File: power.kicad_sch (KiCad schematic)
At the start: 40 parts, among them T1 net-tie, U2 TPS546D24ARVFR

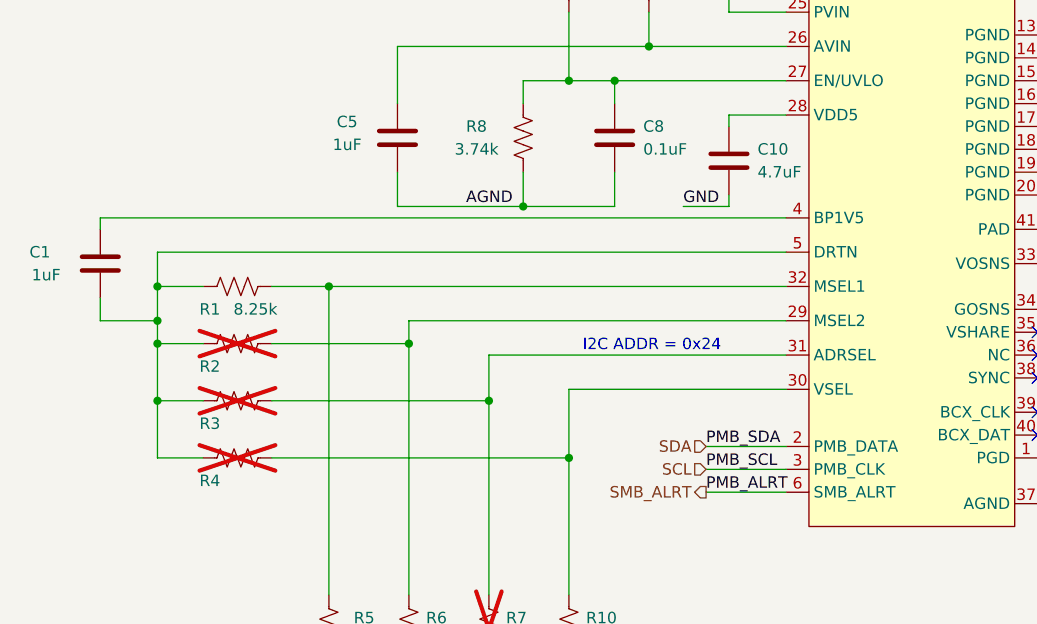
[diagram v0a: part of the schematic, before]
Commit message: swapped some parts numbers and packages for #169, DFM Improvements
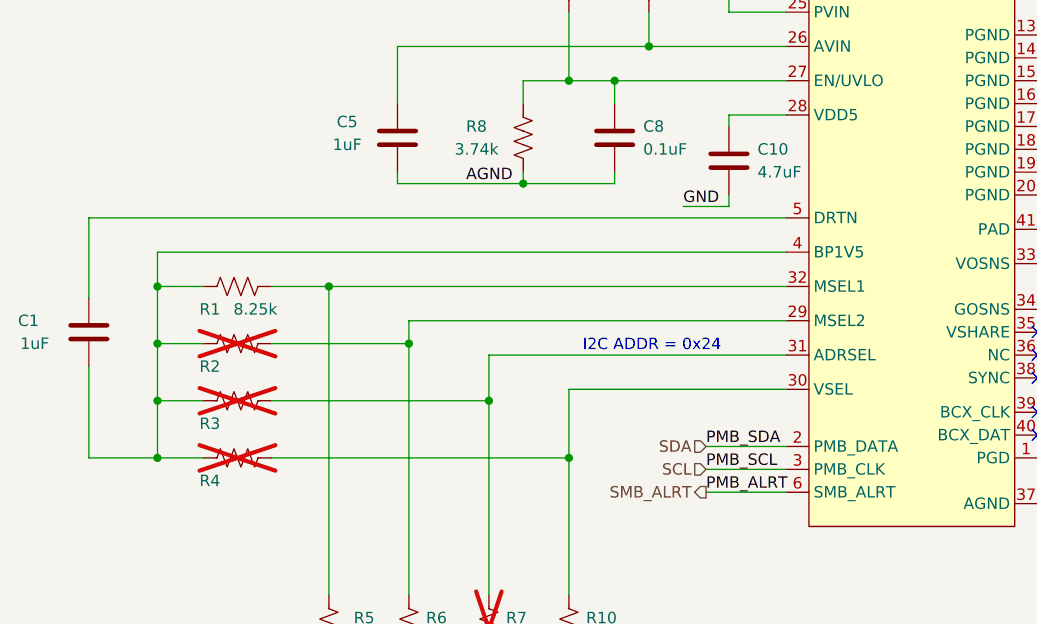
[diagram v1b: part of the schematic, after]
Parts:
- C1: footprint Capacitor_SMD:C_0603_1608Metric -> Capacitor_SMD:C_0402_1005Metric; DK 490-1550-1-ND -> 587-5514-1-ND; PARTNO GRM188R60J105KA01D -> EMK105BJ105MV-F
- C17, C18, C19, C20: footprint Capacitor_SMD:C_1210_3225Metric -> Capacitor_SMD:C_1206_3216Metric; DK 490-6533-1-ND -> 445-6008-1-ND; PARTNO GRM32EC80J107ME20L -> C3216X5R0J107M160AB
- C2: footprint Capacitor_SMD:C_1206_3216Metric -> Capacitor_SMD:C_0805_2012Metric; DK 1276-3038-1-ND -> 1276-1096-1-ND; PARTNO CL31A106KAHNFNE -> CL21A106KOQNNNE
- C5, C7: footprint Capacitor_SMD:C_0805_2012Metric -> Capacitor_SMD:C_0402_1005Metric; DK 587-1291-1-ND -> 587-5514-1-ND; PARTNO TMK212BJ105KG-T -> EMK105BJ105MV-F
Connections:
- net at C1.1: now also U2.5 (DRTN); no longer U2.4 (BP1V5)
- net at C1.2, R1.1, R2.1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: now also U2.4 (BP1V5); no longer U2.5 (DRTN)
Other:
- moved on the sheet: C1

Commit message: silkscreen cleanup
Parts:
- C17, C18, C19, C20: DK 445-6008-1-ND -> 490-GRM31CR61A107MEA8LCT-ND; PARTNO C3216X5R0J107M160AB -> GRM31CR61A107MEA8L
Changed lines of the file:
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@@
 			)
 		)
-		(property "DK" "445-6008-1-ND"
+		(property "DK" "490-GRM31CR61A107MEA8LCT-ND"
 			(at 224.79 68.58 0)
 			(effects
@@
 			)
 		)
-		(property "PARTNO" "C3216X5R0J107M160AB"
+		(property "PARTNO" "GRM31CR61A107MEA8L"
 			(at 224.79 68.58 0)
 			(effects
@@
 			)
 		)
-		(property "DK" "445-6008-1-ND"
+		(property "DK" "490-GRM31CR61A107MEA8LCT-ND"
 			(at 214.63 60.96 0)
 			(effects
@@
 			)
 		)
-		(property "PARTNO" "C3216X5R0J107M160AB"
+		(property "PARTNO" "GRM31CR61A107MEA8L"
 			(at 214.63 60.96 0)
 			(effects
@@
 			)
 		)
-		(property "DK" "445-6008-1-ND"
+		(property "DK" "490-GRM31CR61A107MEA8LCT-ND"
 			(at 234.95 60.96 0)
 			(effects
@@
 			)
 		)
-		(property "PARTNO" "C3216X5R0J107M160AB"
+		(property "PARTNO" "GRM31CR61A107MEA8L"
 			(at 234.95 60.96 0)
 			(effects
@@
 			)
 		)
-		(property "DK" "445-6008-1-ND"
+		(property "DK" "490-GRM31CR61A107MEA8LCT-ND"
 			(at 204.47 68.58 0)
 			(effects
@@
 			)
 		)
-		(property "PARTNO" "C3216X5R0J107M160AB"
+		(property "PARTNO" "GRM31CR61A107MEA8L"
 			(at 204.47 68.58 0)
 			(effects

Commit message: caps, back plane
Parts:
- C16: DK 490-10746-1-ND -> 490-10746-2-ND
- C17, C18, C19, C20: DK 490-GRM31CR61A107MEA8LCT-ND -> 1276-1782-2-ND; PARTNO GRM31CR61A107MEA8L -> CL31A107MQHNNNE
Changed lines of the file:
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@@
 			)
 		)
-		(property "DK" "490-GRM31CR61A107MEA8LCT-ND"
+		(property "DK" "1276-1782-2-ND"
 			(at 224.79 68.58 0)
 			(effects
@@
 			)
 		)
-		(property "PARTNO" "GRM31CR61A107MEA8L"
+		(property "PARTNO" "CL31A107MQHNNNE"
 			(at 224.79 68.58 0)
 			(effects
@@
 			)
 		)
-		(property "DK" "490-GRM31CR61A107MEA8LCT-ND"
+		(property "DK" "1276-1782-2-ND"
 			(at 214.63 60.96 0)
 			(effects
@@
 			)
 		)
-		(property "PARTNO" "GRM31CR61A107MEA8L"
+		(property "PARTNO" "CL31A107MQHNNNE"
 			(at 214.63 60.96 0)
 			(effects
@@
 			)
 		)
-		(property "DK" "490-GRM31CR61A107MEA8LCT-ND"
+		(property "DK" "1276-1782-2-ND"
 			(at 234.95 60.96 0)
 			(effects
@@
 			)
 		)
-		(property "PARTNO" "GRM31CR61A107MEA8L"
+		(property "PARTNO" "CL31A107MQHNNNE"
 			(at 234.95 60.96 0)
 			(effects
@@
 			)
 		)
-		(property "DK" "490-10746-1-ND"
+		(property "DK" "490-10746-2-ND"
 			(at 195.58 60.96 0)
 			(effects
@@
 			)
 		)
-		(property "DK" "490-GRM31CR61A107MEA8LCT-ND"
+		(property "DK" "1276-1782-2-ND"
 			(at 204.47 68.58 0)
 			(effects
@@
 			)
 		)
-		(property "PARTNO" "GRM31CR61A107MEA8L"
+		(property "PARTNO" "CL31A107MQHNNNE"
 			(at 204.47 68.58 0)
 			(effects

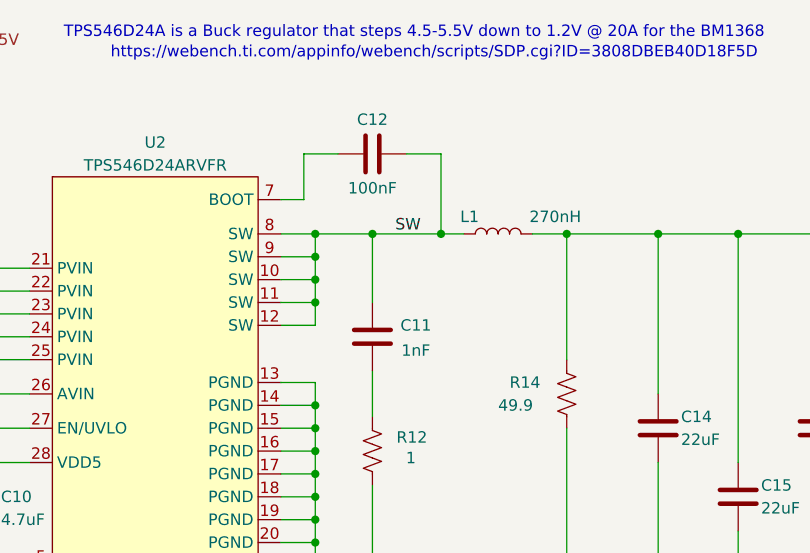
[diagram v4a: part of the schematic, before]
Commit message: normalized 0.1uF capacitor part numbers
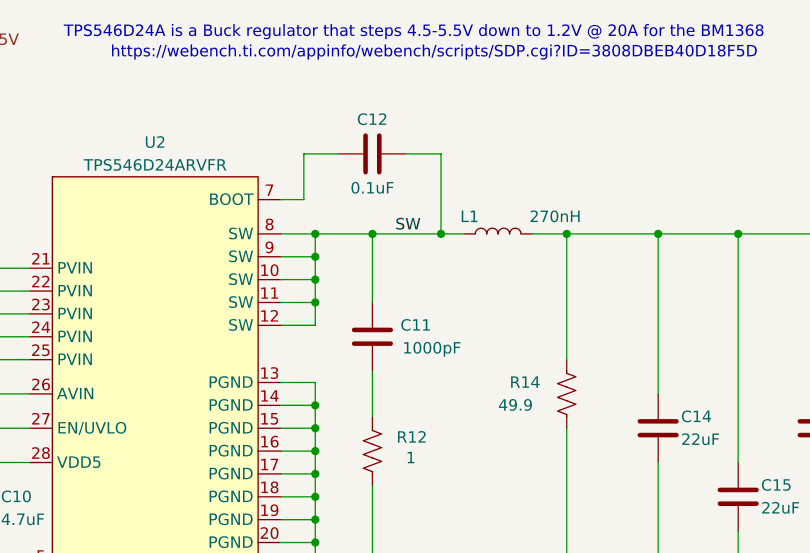
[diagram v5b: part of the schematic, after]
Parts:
- C11: value 1nF -> 1000pF
- C12: value 100nF -> 0.1uF; footprint Capacitor_SMD:C_0805_2012Metric -> Capacitor_SMD:C_0402_1005Metric; DK 478-KGM21NR71E104KTCT-ND -> 1276-1234-1-ND; PARTNO KGM21NR71E104KT -> CL05A104KO5NNNC
- C16: DK 490-10746-2-ND -> 490-10746-1-ND
- C8: DK 1292-1639-1-ND -> 1276-1234-1-ND; PARTNO 0402X104K100CT -> CL05A104KO5NNNC
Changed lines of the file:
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@@
 			)
 		)
-		(property "Value" "1nF"
-			(at 150.876 52.324 0)
+		(property "Value" "1000pF"
+			(at 152.654 52.07 0)
 			(effects
 				(font
@@
 			)
 		)
-		(property "Value" "100nF"
+		(property "Value" "0.1uF"
 			(at 146.05 34.29 90)
 			(effects
@@
 			)
 		)
-		(property "Footprint" "Capacitor_SMD:C_0805_2012Metric"
+		(property "Footprint" "Capacitor_SMD:C_0402_1005Metric"
 			(at 149.86 29.5148 0)
 			(effects
@@
 			)
 		)
-		(property "DK" "478-KGM21NR71E104KTCT-ND"
+		(property "DK" "1276-1234-1-ND"
 			(at 146.05 30.48 0)
 			(effects
@@
 			)
 		)
-		(property "PARTNO" "KGM21NR71E104KT"
+		(property "PARTNO" "CL05A104KO5NNNC"
 			(at 146.05 30.48 0)
 			(effects
@@
 			)
 		)
-		(property "DK" "1292-1639-1-ND"
+		(property "DK" "1276-1234-1-ND"
 			(at 88.9 67.31 0)
 			(effects
@@
 			)
 		)
-		(property "PARTNO" "0402X104K100CT"
+		(property "PARTNO" "CL05A104KO5NNNC"
 			(at 88.9 67.31 0)
 			(effects
@@
 			)
 		)
-		(property "DK" "490-10746-2-ND"
+		(property "DK" "490-10746-1-ND"
 			(at 195.58 60.96 0)
 			(effects

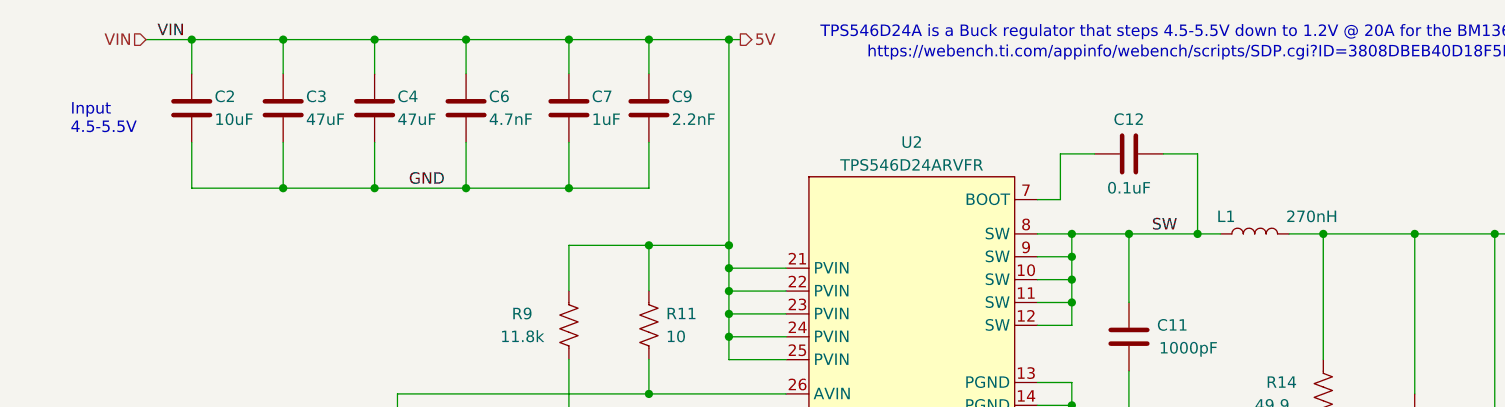
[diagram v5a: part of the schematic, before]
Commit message: change C43 to 100uF
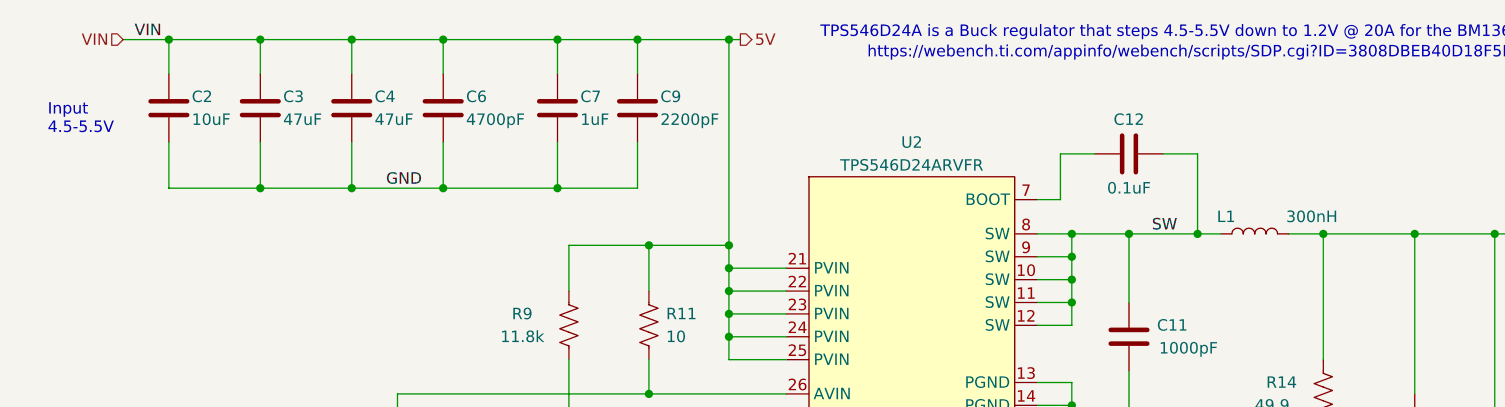
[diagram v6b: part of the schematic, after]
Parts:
- C6: value 4.7nF -> 4700pF
- C9: value 2.2nF -> 2200pF
- L1: value 270nH -> 300nH; PARTNO SLC1175-271MEC -> SLC1175-301MEC
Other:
- moved on the sheet: C2, C3, C4, C6, C7, C9

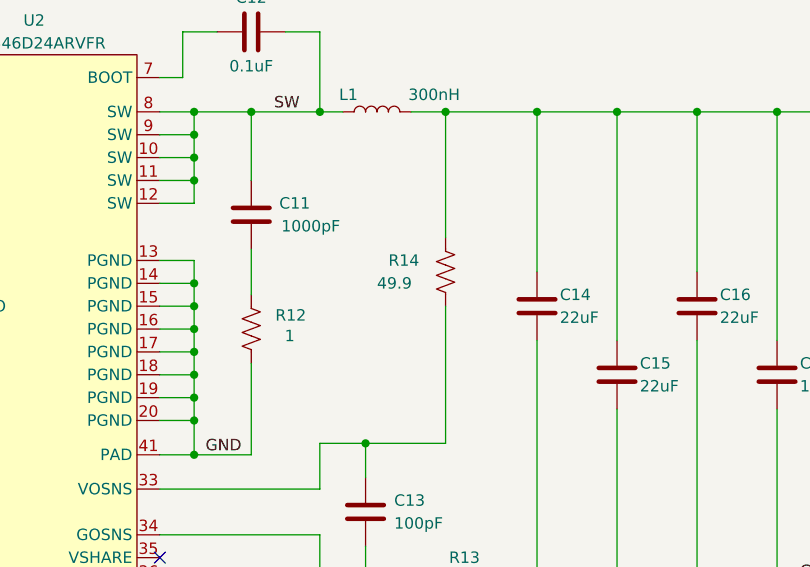
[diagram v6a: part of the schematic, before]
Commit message: fixed 25MHz oscillator package name and part number in project and BOM
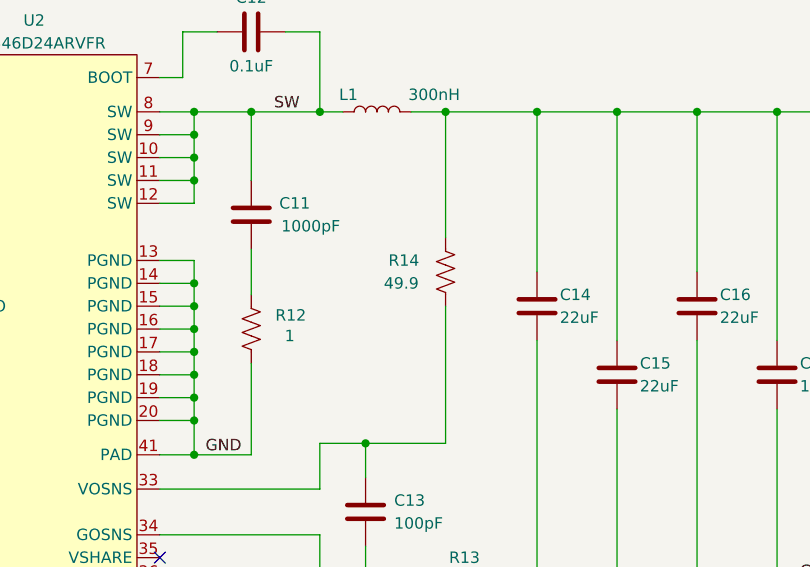
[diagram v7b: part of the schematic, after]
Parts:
- L1: footprint bitaxe:SLC1175-271MEC_COC -> bitaxe:SLC1175; Mouser 994-SLC1175-271MEC -> 994-SLC1175-301MEC
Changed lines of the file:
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@@
 		)
 		(property "Value" "49.9"
-			(at 160.02 58.42 0)
+			(at 160.782 58.42 0)
 			(effects
 				(font
@@
 			)
 		)
-		(property "Footprint" "bitaxe:SLC1175-271MEC_COC"
+		(property "Footprint" "bitaxe:SLC1175"
 			(at 160.02 39.37 0)
 			(effects
@@
 			)
 		)
-		(property "Mouser" "994-SLC1175-271MEC"
+		(property "Mouser" "994-SLC1175-301MEC"
 			(at 160.02 39.37 90)
 			(effects
@@
 		)
 	)
+	(sheet_instances
+		(path "/"
+			(page "1")
+		)
+	)

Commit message: misc
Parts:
- removed R2, R3, R4, R7: ~, Resistor_SMD:R_0402_1005Metric, symbol Device:R_US
